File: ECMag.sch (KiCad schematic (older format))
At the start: 48 parts, among them J1 Conn_01x12, J2 Conn_01x05, J3 Conn_01x04, J4 USB_B, J5 Barrel_Jack_SW, J6 Conn_01x04, K1 Tactil Switch B3F NA, K2 Tactil Switch B3F NA, K3 Tactil Switch B3F NA, K4 Tactil Switch B3F NA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

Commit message: cambio de huellas del pulsador
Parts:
- K1, K2, K3, K4: footprint EMS_huellas:SW_6x5mm_2C -> Button_Switch_THT:SW_PUSH_6mm_H5mm; Digikey Z7863CT-ND -> B3F-1060
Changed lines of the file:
@@
 Wire Wire Line
 	4850 2550 4850 2650
-$Comp
-L Enc_Mag:NA K1
-U 1 1 5ED39BE4
-P 4850 2850
-F 0 "K1" V 4850 2807 50  0000 R CNN
-F 1 "Tactil Switch B3F NA" V 4895 2806 50  0001 R CNN
-F 2 "EMS_huellas:SW_6x5mm_2C" H 4775 3025 50  0001 C CNN
-F 3 "https://www.digikey.com/product-detail/es/omron-electronics-inc-emc-div/B3F-6025/Z7863CT-ND/7612384" H 4775 3025 50  0001 C CNN
-F 4 "Z7863CT-ND" V 4850 2850 50  0001 C CNN "Digikey"
-	1    4850 2850
-	0    -1   1    0
-$EndComp
 Wire Wire Line
 	5200 6100 5200 5850
@@
 F 0 "K2" V 7950 2807 50  0000 R CNN
 F 1 "Tactil Switch B3F NA" V 7995 2806 50  0001 R CNN
-F 2 "EMS_huellas:SW_6x5mm_2C" H 7875 3025 50  0001 C CNN
+F 2 "Button_Switch_THT:SW_PUSH_6mm_H5mm" H 7875 3025 50  0001 C CNN
 F 3 "https://www.digikey.com/product-detail/es/omron-electronics-inc-emc-div/B3F-6025/Z7863CT-ND/7612384" H 7875 3025 50  0001 C CNN
-F 4 "Z7863CT-ND" V 7950 2850 50  0001 C CNN "Digikey"
+F 4 "B3F-1060" V 7950 2850 50  0001 C CNN "Digikey"
 	1    7950 2850
 	0    -1   1    0
@@
 Wire Wire Line
 	8650 2550 8250 2550
-$Comp
-L Enc_Mag:NA K3
-U 1 1 5ED8724C
-P 1200 6800
-F 0 "K3" V 1200 6757 50  0000 R CNN
-F 1 "Tactil Switch B3F NA" V 1245 6756 50  0001 R CNN
-F 2 "EMS_huellas:SW_6x5mm_2C" H 1125 6975 50  0001 C CNN
-F 3 "https://www.digikey.com/product-detail/es/omron-electronics-inc-emc-div/B3F-6025/Z7863CT-ND/7612384" H 1125 6975 50  0001 C CNN
-F 4 "Z7863CT-ND" V 1200 6800 50  0001 C CNN "Digikey"
-	1    1200 6800
-	0    -1   1    0
-$EndComp
 Wire Wire Line
 	1200 7000 1200 7100
@@
 	1    1200 7100
 	1    0    0    -1
-$EndComp
-$Comp
-L Enc_Mag:NA K4
-U 1 1 5EDA5472
-P 1550 6800
-F 0 "K4" V 1550 6757 50  0000 R CNN
-F 1 "Tactil Switch B3F NA" V 1595 6756 50  0001 R CNN
-F 2 "EMS_huellas:SW_6x5mm_2C" H 1475 6975 50  0001 C CNN
-F 3 "https://www.digikey.com/product-detail/es/omron-electronics-inc-emc-div/B3F-6025/Z7863CT-ND/7612384" H 1475 6975 50  0001 C CNN
-F 4 "Z7863CT-ND" V 1550 6800 50  0001 C CNN "Digikey"
-	1    1550 6800
-	0    -1   1    0
 $EndComp
 Wire Wire Line
@@
 Text Notes 5650 4950 0    50   ~ 0
 Adquisicion de datos y \nmanejo de interfaces
+$Comp
+L Enc_Mag:NA K1
+U 1 1 5F0165AB
+P 4850 2850
+F 0 "K1" V 4850 2807 50  0000 R CNN
+F 1 "Tactil Switch B3F NA" V 4895 2806 50  0001 R CNN
+F 2 "Button_Switch_THT:SW_PUSH_6mm_H5mm" H 4775 3025 50  0001 C CNN
+F 3 "https://www.digikey.com/product-detail/es/omron-electronics-inc-emc-div/B3F-6025/Z7863CT-ND/7612384" H 4775 3025 50  0001 C CNN
+F 4 "B3F-1060" V 4850 2850 50  0001 C CNN "Digikey"
+	1    4850 2850
+	0    -1   1    0
+$EndComp
+$Comp
+L Enc_Mag:NA K4
+U 1 1 5F030342
+P 1550 6800
+F 0 "K4" V 1550 6757 50  0000 R CNN
+F 1 "Tactil Switch B3F NA" V 1595 6756 50  0001 R CNN
+F 2 "Button_Switch_THT:SW_PUSH_6mm_H5mm" H 1475 6975 50  0001 C CNN
+F 3 "https://www.digikey.com/product-detail/es/omron-electronics-inc-emc-div/B3F-6025/Z7863CT-ND/7612384" H 1475 6975 50  0001 C CNN
+F 4 "B3F-1060" V 1550 6800 50  0001 C CNN "Digikey"
+	1    1550 6800
+	0    -1   1    0
+$EndComp
+$Comp
+L Enc_Mag:NA K3
+U 1 1 5F0336CA
+P 1200 6800
+F 0 "K3" V 1200 6757 50  0000 R CNN
+F 1 "Tactil Switch B3F NA" V 1245 6756 50  0001 R CNN
+F 2 "Button_Switch_THT:SW_PUSH_6mm_H5mm" H 1125 6975 50  0001 C CNN
+F 3 "https://www.digikey.com/product-detail/es/omron-electronics-inc-emc-div/B3F-6025/Z7863CT-ND/7612384" H 1125 6975 50  0001 C CNN
+F 4 "B3F-1060" V 1200 6800 50  0001 C CNN "Digikey"
+	1    1200 6800
+	0    -1   1    0
+$EndComp
 Wire Bus Line
 	8300 3950 8300 4200

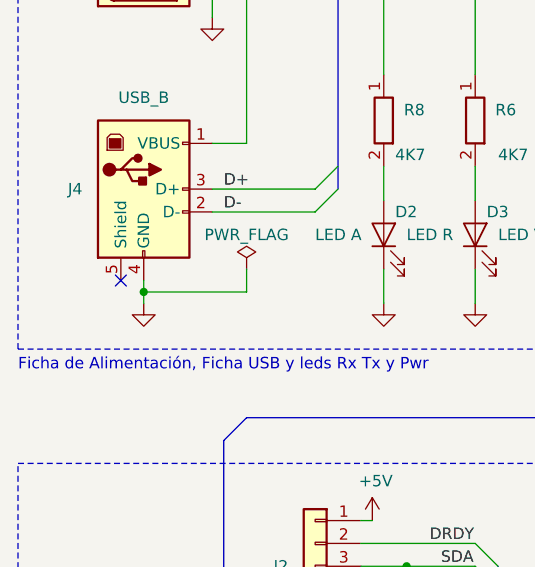
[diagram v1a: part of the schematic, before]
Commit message: Paso de los tracks de 0.25 a 0.45, tracks de senhales y potencia
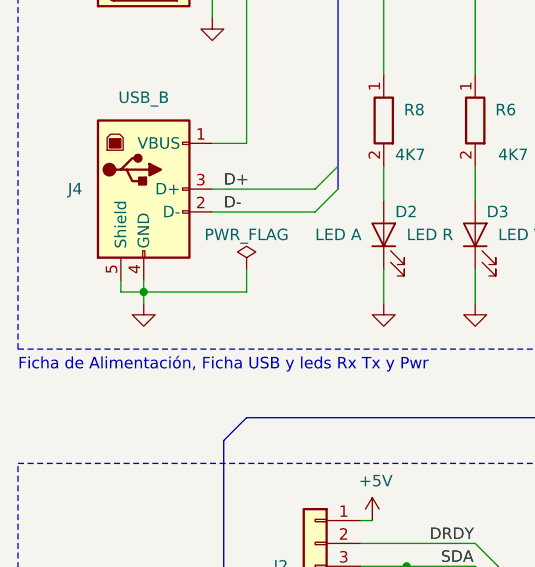
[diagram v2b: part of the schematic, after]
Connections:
- net GND: now also J4.5 (Shield)
- no-connect marks 18 -> 17
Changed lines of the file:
@@
 	3850 5850 3850 5800
 Connection ~ 3850 5850
-NoConn ~ 1400 2750
 $Comp
 L Enc_Mag:Resistencia R10
@@
 	0    -1   1    0
 $EndComp
+Wire Wire Line
+	1400 2750 1400 2800
+Wire Wire Line
+	1400 2800 1500 2800
 Wire Bus Line
 	8300 3950 8300 4200

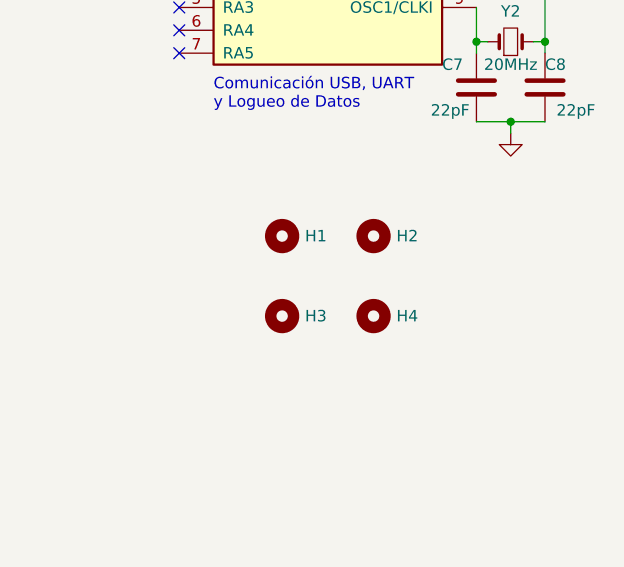
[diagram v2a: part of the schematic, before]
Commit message: Agregadas las imagenes 3D del power jack y del USB B, corregidas esquinas del pcb, agregados fiduciarios, parametros del circuito, grilla, datos del fabricante, dimensiones del pcb, datos de serigrafía, cambiada la licencia por la de BSD Modificada
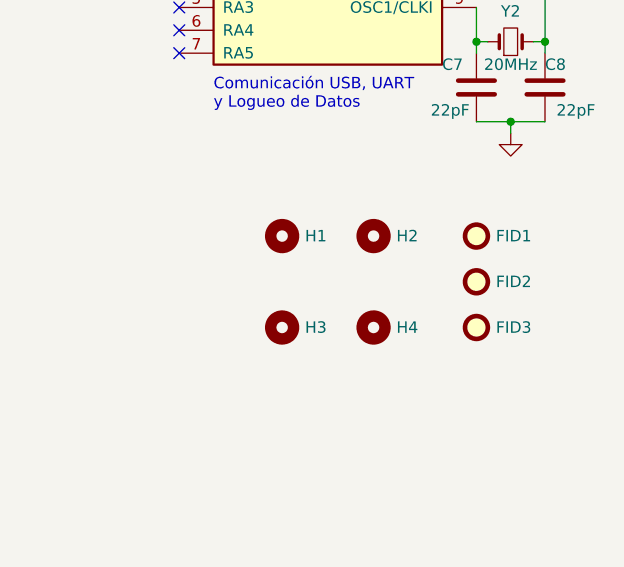
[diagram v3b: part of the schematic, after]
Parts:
- added FID1, FID2, FID3: Fiducial, Fiducial:Fiducial_1mm_Mask2mm, symbol Mechanical:Fiducial
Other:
- moved on the sheet: H3, H4
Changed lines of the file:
@@
 encoding utf-8
 Sheet 1 1
-Title "Escaner Campos Magnéticos de Superficies para Soldaduras"
+Title "Escáner de campos magnéticos superficiales para soldaduras"
 Date "2020-05-11"
 Rev "1.8"
 Comp "Pablo J.C. Alonso Castilllo"
 Comment1 "Revisor: Mauricio Barroso Benavidez"
-Comment2 "Esta obra está bajo una Licencia Creative Commons Atribución 4.0 Internacional."
+Comment2 "Esta obra está bajo licencia BSD Modificada - https://es.wikipedia.org/wiki/Licencia_BSD"
 Comment3 "CESE 10º Cohorte"
 Comment4 "Diseño de Circuitos Impresos"
@@
 L Mechanical:MountingHole H3
 U 1 1 5EDE3BFF
-P 9100 5850
-F 0 "H3" H 9200 5850 50  0000 L CNN
-F 1 "MountingHole" H 9200 5805 50  0001 L CNN
-F 2 "MountingHole:MountingHole_3.2mm_M3" H 9100 5850 50  0001 C CNN
-F 3 "~" H 9100 5850 50  0001 C CNN
-	1    9100 5850
+P 9100 5900
+F 0 "H3" H 9200 5900 50  0000 L CNN
+F 1 "MountingHole" H 9200 5855 50  0001 L CNN
+F 2 "MountingHole:MountingHole_3.2mm_M3" H 9100 5900 50  0001 C CNN
+F 3 "~" H 9100 5900 50  0001 C CNN
+	1    9100 5900
 	1    0    0    -1
 $EndComp
@@
 L Mechanical:MountingHole H4
 U 1 1 5EDE3C09
-P 9500 5850
-F 0 "H4" H 9600 5850 50  0000 L CNN
-F 1 "MountingHole" H 9600 5805 50  0001 L CNN
-F 2 "MountingHole:MountingHole_3.2mm_M3" H 9500 5850 50  0001 C CNN
-F 3 "~" H 9500 5850 50  0001 C CNN
-	1    9500 5850
+P 9500 5900
+F 0 "H4" H 9600 5900 50  0000 L CNN
+F 1 "MountingHole" H 9600 5855 50  0001 L CNN
+F 2 "MountingHole:MountingHole_3.2mm_M3" H 9500 5900 50  0001 C CNN
+F 3 "~" H 9500 5900 50  0001 C CNN
+	1    9500 5900
 	1    0    0    -1
 $EndComp
@@
 Wire Bus Line
 	4250 4000 4250 4900
+$Comp
+L Mechanical:Fiducial FID1
+U 1 1 5EFEFF87
+P 9950 5500
+F 0 "FID1" H 10035 5500 50  0000 L CNN
+F 1 "Fiducial" H 10035 5455 50  0001 L CNN
+F 2 "Fiducial:Fiducial_1mm_Mask2mm" H 9950 5500 50  0001 C CNN
+F 3 "~" H 9950 5500 50  0001 C CNN
+	1    9950 5500
+	1    0    0    -1
+$EndComp
+$Comp
+L Mechanical:Fiducial FID2
+U 1 1 5EFF0DEB
+P 9950 5700
+F 0 "FID2" H 10035 5700 50  0000 L CNN
+F 1 "Fiducial" H 10035 5655 50  0001 L CNN
+F 2 "Fiducial:Fiducial_1mm_Mask2mm" H 9950 5700 50  0001 C CNN
+F 3 "~" H 9950 5700 50  0001 C CNN
+	1    9950 5700
+	1    0    0    -1
+$EndComp
+$Comp
+L Mechanical:Fiducial FID3
+U 1 1 5EFF195F
+P 9950 5900
+F 0 "FID3" H 10035 5900 50  0000 L CNN
+F 1 "Fiducial" H 10035 5855 50  0001 L CNN
+F 2 "Fiducial:Fiducial_1mm_Mask2mm" H 9950 5900 50  0001 C CNN
+F 3 "~" H 9950 5900 50  0001 C CNN
+	1    9950 5900
+	1    0    0    -1
+$EndComp
 $EndSCHEMATC

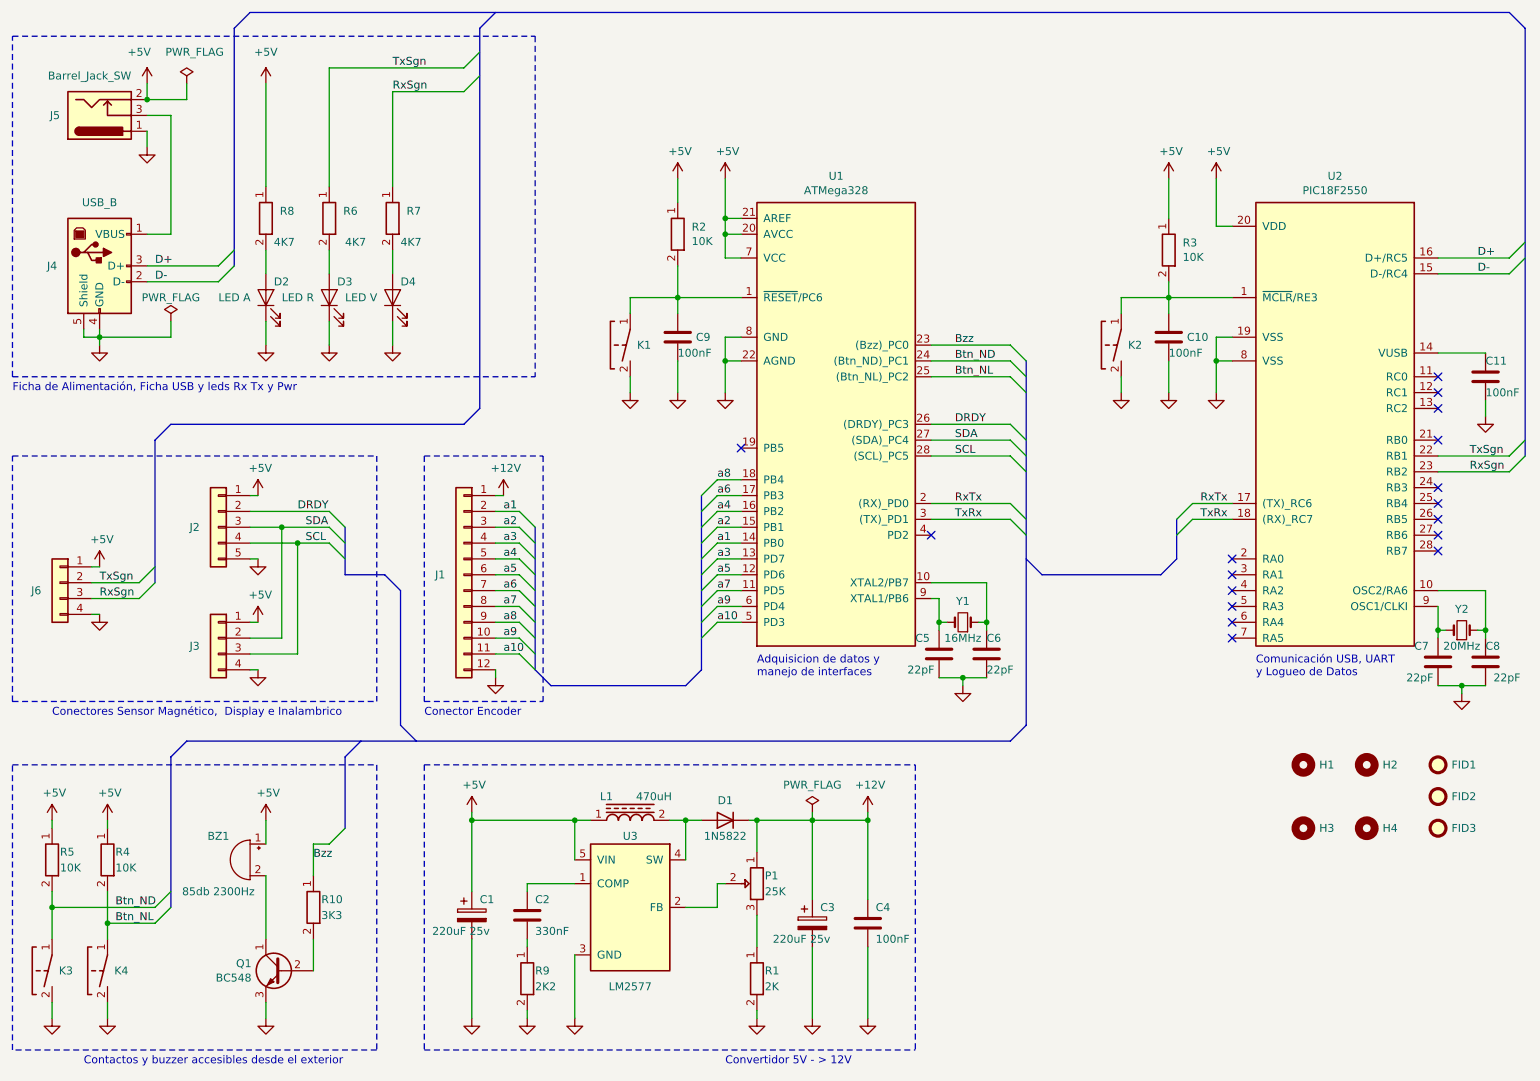
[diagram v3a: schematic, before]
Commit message: 1.- Reemplaxado K por Sw en el esquemático.
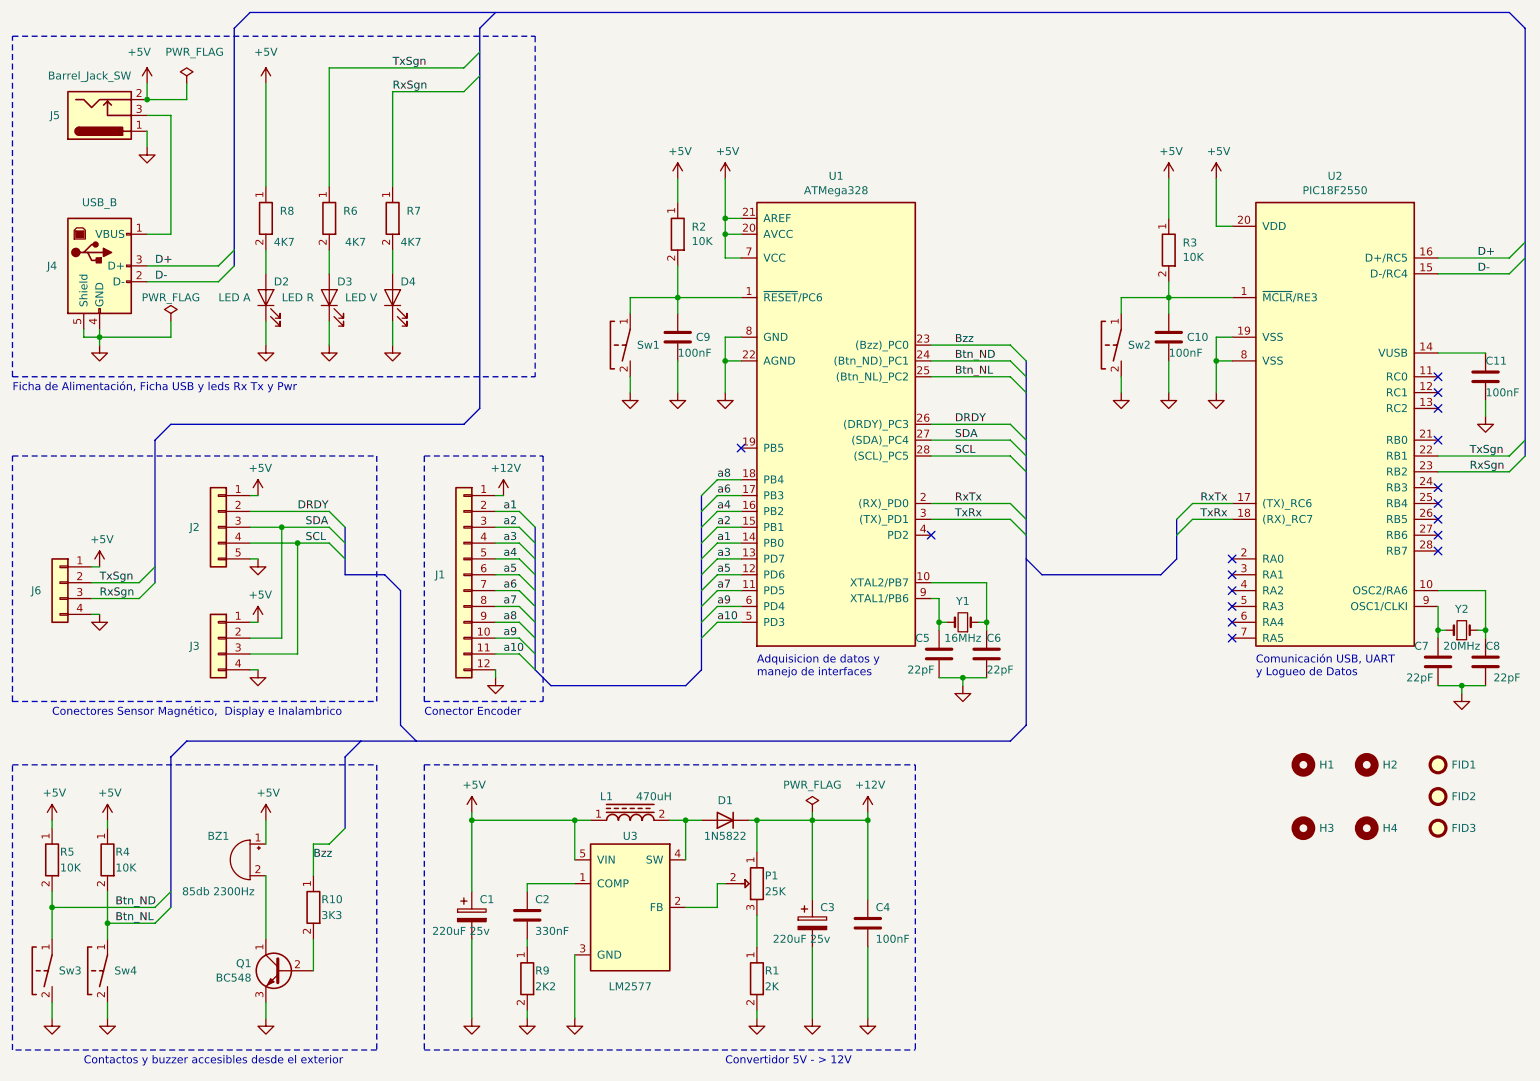
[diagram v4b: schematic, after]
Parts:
- renumbered K1 to Sw1, K2 to Sw2, K3 to Sw3, K4 to Sw4
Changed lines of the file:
@@
 $EndComp
 $Comp
-L Enc_Mag:NA K2
+L Enc_Mag:NA Sw2
 U 1 1 5EBC7DA1
 P 7950 2850
-F 0 "K2" V 7950 2807 50  0000 R CNN
+F 0 "Sw2" V 7950 2807 50  0000 R CNN
 F 1 "Tactil Switch B3F NA" V 7995 2806 50  0001 R CNN
 F 2 "Button_Switch_THT:SW_PUSH_6mm_H5mm" H 7875 3025 50  0001 C CNN
@@
 Adquisicion de datos y \nmanejo de interfaces
 $Comp
-L Enc_Mag:NA K1
+L Enc_Mag:NA Sw1
 U 1 1 5F0165AB
 P 4850 2850
-F 0 "K1" V 4850 2807 50  0000 R CNN
+F 0 "Sw1" V 4850 2807 50  0000 R CNN
 F 1 "Tactil Switch B3F NA" V 4895 2806 50  0001 R CNN
 F 2 "Button_Switch_THT:SW_PUSH_6mm_H5mm" H 4775 3025 50  0001 C CNN
@@
 $EndComp
 $Comp
-L Enc_Mag:NA K4
+L Enc_Mag:NA Sw4
 U 1 1 5F030342
 P 1550 6800
-F 0 "K4" V 1550 6757 50  0000 R CNN
+F 0 "Sw4" V 1550 6757 50  0000 R CNN
 F 1 "Tactil Switch B3F NA" V 1595 6756 50  0001 R CNN
 F 2 "Button_Switch_THT:SW_PUSH_6mm_H5mm" H 1475 6975 50  0001 C CNN
@@
 $EndComp
 $Comp
-L Enc_Mag:NA K3
+L Enc_Mag:NA Sw3
 U 1 1 5F0336CA
 P 1200 6800
-F 0 "K3" V 1200 6757 50  0000 R CNN
+F 0 "Sw3" V 1200 6757 50  0000 R CNN
 F 1 "Tactil Switch B3F NA" V 1245 6756 50  0001 R CNN
 F 2 "Button_Switch_THT:SW_PUSH_6mm_H5mm" H 1125 6975 50  0001 C CNN
@@
 Wire Wire Line
 	1400 2800 1500 2800
-Wire Bus Line
-	8300 3950 8300 4200
-Wire Bus Line
-	1950 5450 1950 6400
-Wire Bus Line
-	1850 3450 1850 4350
-Wire Bus Line
-	2350 850  2350 2350
-Wire Bus Line
-	2450 750  10400 750
-Wire Bus Line
-	3050 4000 3050 4300
-Wire Bus Line
-	2050 5350 7250 5350
-Wire Bus Line
-	3900 850  3900 3250
-Wire Bus Line
-	10500 850  10500 3550
-Wire Bus Line
-	7350 2950 7350 5250
-Wire Bus Line
-	5300 3800 5300 4900
-Wire Bus Line
-	4250 4000 4250 4900
 $Comp
 L Mechanical:Fiducial FID1
@@
 	1    0    0    -1
 $EndComp
+Wire Bus Line
+	8300 3950 8300 4200
+Wire Bus Line
+	1950 5450 1950 6400
+Wire Bus Line
+	1850 3450 1850 4350
+Wire Bus Line
+	2350 850  2350 2350
+Wire Bus Line
+	2450 750  10400 750
+Wire Bus Line
+	3050 4000 3050 4300
+Wire Bus Line
+	2050 5350 7250 5350
+Wire Bus Line
+	3900 850  3900 3250
+Wire Bus Line
+	10500 850  10500 3550
+Wire Bus Line
+	7350 2950 7350 5250
+Wire Bus Line
+	5300 3800 5300 4900
+Wire Bus Line
+	4250 4000 4250 4900
 $EndSCHEMATC
